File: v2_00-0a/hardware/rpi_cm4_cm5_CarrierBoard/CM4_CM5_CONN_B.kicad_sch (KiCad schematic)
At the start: 2 parts, among them J7 DF40HC(3.0)-100DS-0.4V(58), U17 Raspberry PI CM4 and CM5 symb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

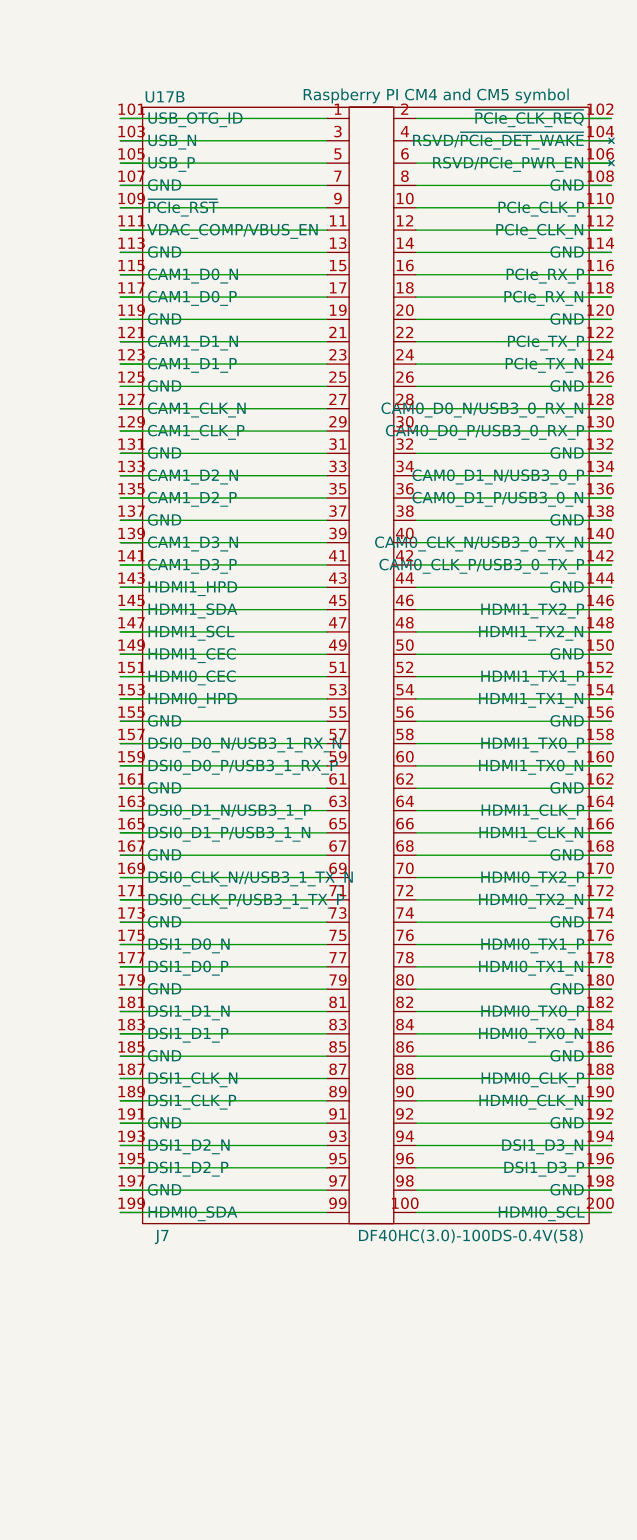
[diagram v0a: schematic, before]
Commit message: Update schematics (several new hierarchical pages, updates bus labels)
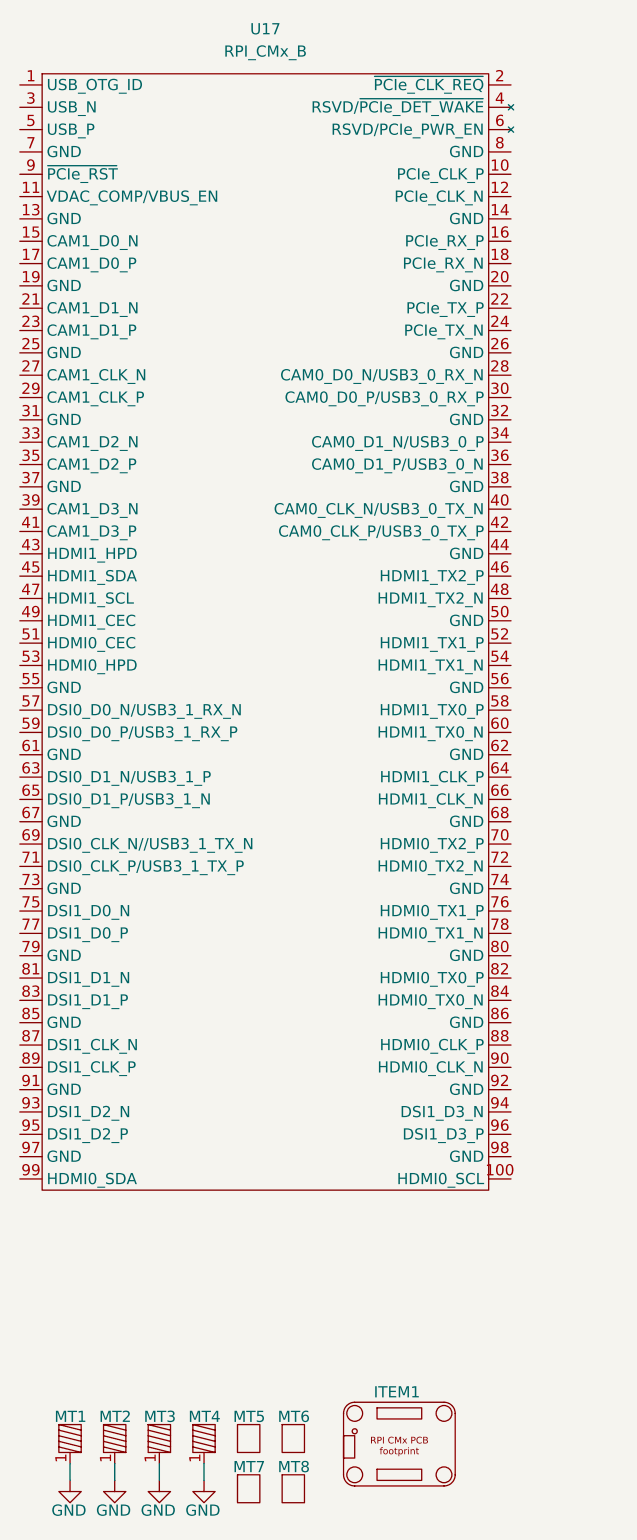
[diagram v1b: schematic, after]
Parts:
- removed J7: DF40HC(3.0)-100DS-0.4V(58), footprint:DF40HC(3.0)-100DS-0.4V, symbol KicadCompDb:Connector/CONN_00007
- removed U17: Raspberry PI CM4 and CM5 symbol, rPI_CM4_CM5, symbol KiCad_Lib_Symbols:RPI_CM4_CM5
- added ITEM1: Raspberry PI CM4 and CM5 symbol, rPI_CM4_CM5, symbol KiCad_Lib_Symbols:RPI_CMx_PCB_FP
- added MT1, MT2, MT3, MT4: 9774030151R, footprint:9774030151R, symbol KicadCompDb:Miscellaneous/MISC_00002
- added MT5, MT6, MT7, MT8: M0504-25-AL-7, footprint:M0504-25-AL-7, symbol KicadCompDb:Miscellaneous/MISC_00004
- added U17: RPI_CMx_B, footprint:DF40HC(3.0)-100DS-0.4V, symbol KicadCompDb:Connector/CONN_00015
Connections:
- new net GND: MT1.1, MT2.1, MT3.1, MT4.1

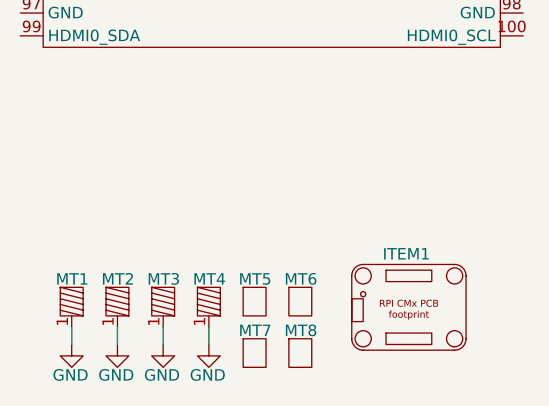
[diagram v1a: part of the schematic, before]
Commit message: Add new page and update schematics
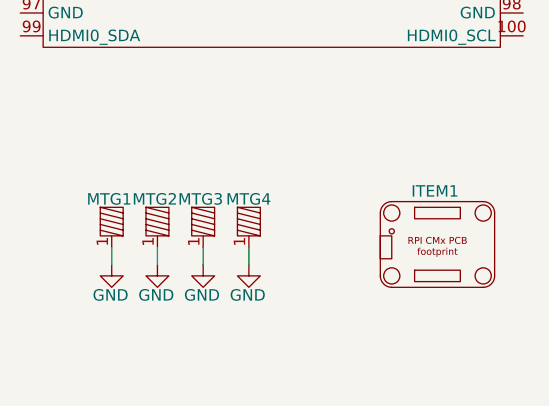
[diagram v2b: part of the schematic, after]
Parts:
- removed MT5, MT6, MT7, MT8: M0504-25-AL-7, footprint:M0504-25-AL-7, symbol KicadCompDb:Miscellaneous/MISC_00004
- renumbered MT1 to MTG1, MT2 to MTG2, MT3 to MTG3, MT4 to MTG4
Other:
- moved on the sheet: ITEM1, MTG1, MTG2, MTG3, MTG4

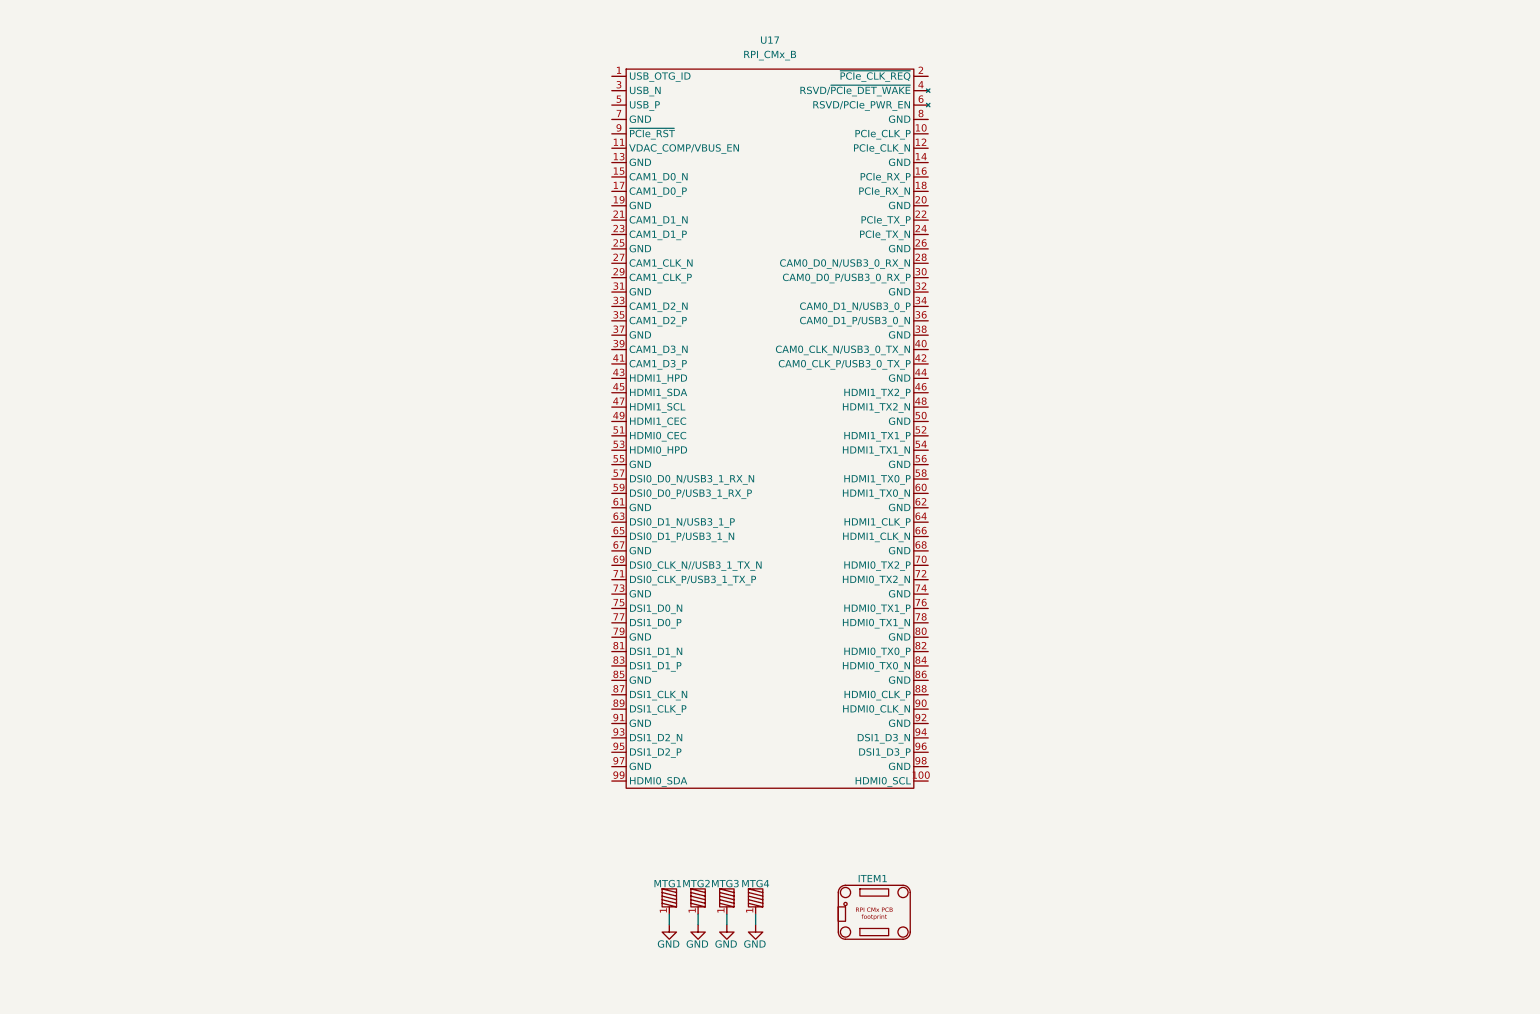
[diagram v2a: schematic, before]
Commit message: Add design notes (power table) and latest changes to power supply and power input
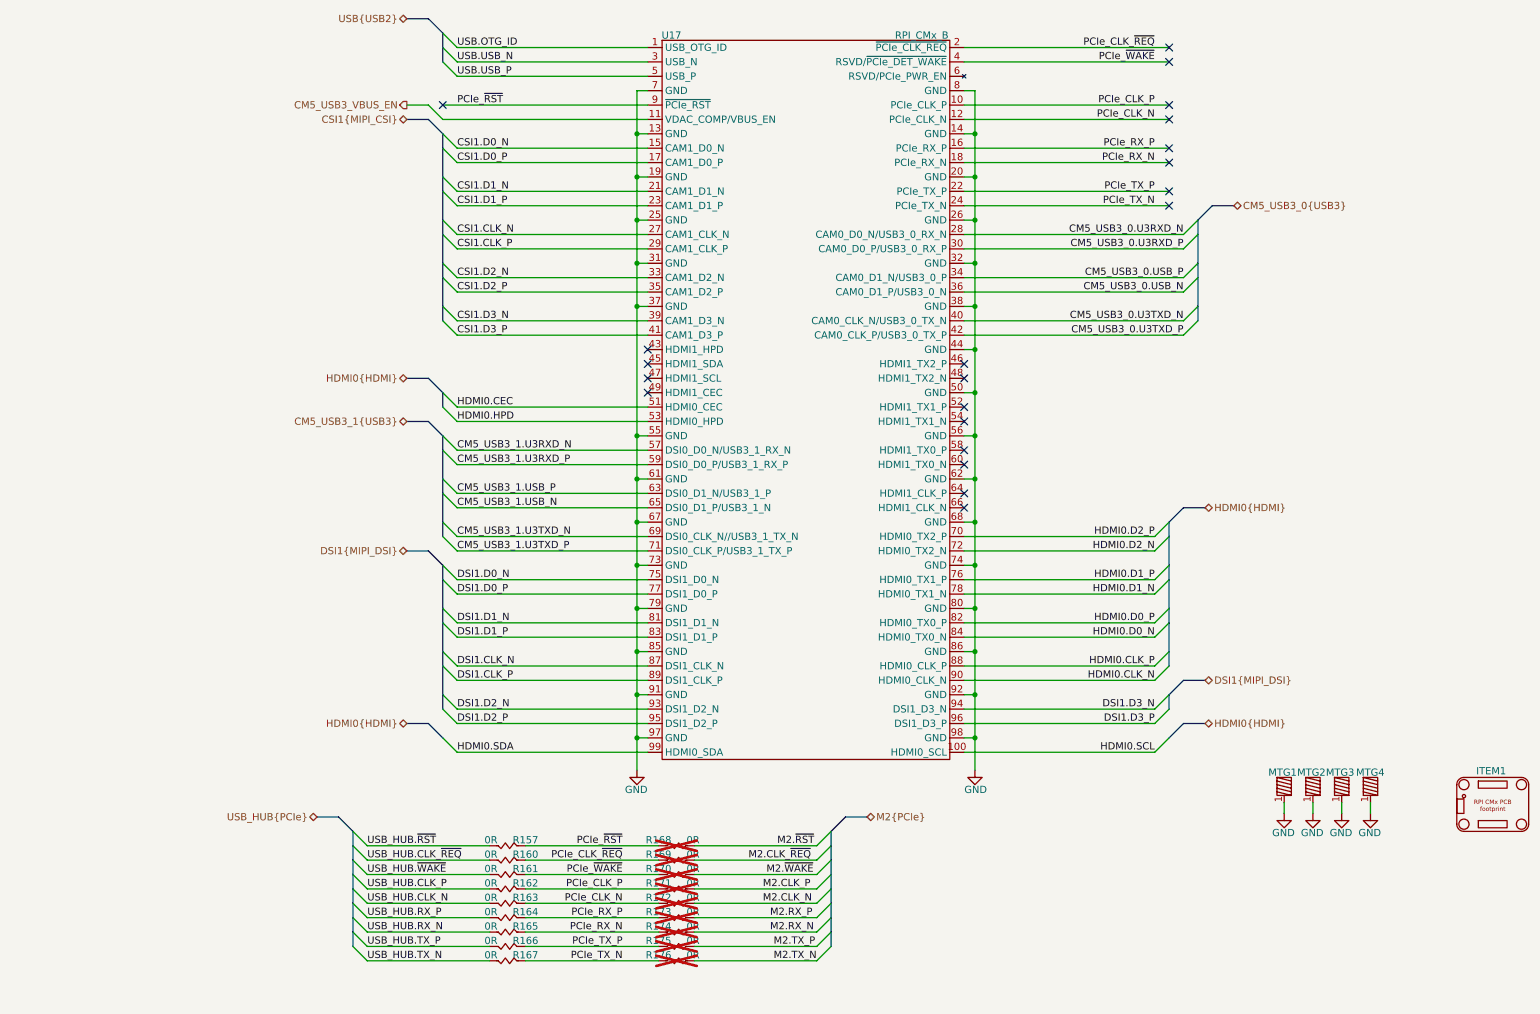
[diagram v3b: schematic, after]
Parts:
- added R157, R160, R161, R162, R163, R164, R165, R166, R167, R168, R169, R170, R171, R172, R173, R174, R175, R176: 0R, footprint:RES_0402, symbol KicadCompDb:Resistors/RES_SMT_00001
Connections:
- net GND: now also U17.13 (GND), U17.14 (GND), U17.19 (GND), U17.20 (GND), U17.25 (GND), U17.26 (GND), U17.31 (GND), U17.32 (GND), U17.37 (GND), U17.38 (GND), U17.44 (GND), U17.50 (GND), U17.55 (GND), U17.56 (GND), U17.61 (GND), U17.62 (GND), U17.67 (GND), U17.68 (GND), U17.7 (GND), U17.73 (GND), U17.74 (GND), U17.79 (GND), U17.8 (GND), U17.80 (GND), U17.85 (GND), U17.86 (GND), U17.91 (GND), U17.92 (GND), U17.97 (GND), U17.98 (GND)
- net USB.OTG_ID: now reaches U17.1 (USB_OTG_ID)
- net PCIe_CLK_P: now reaches U17.10 (PCIe_CLK_P)
- net PCIe_CLK_P: now also R162.1, R171.1
- net HDMI0.SCL: now reaches U17.100 (HDMI0_SCL)
- net CM5_USB3_VBUS_EN: now reaches U17.11 (VDAC_COMP/VBUS_EN)
- net PCIe_CLK_N: now reaches U17.12 (PCIe_CLK_N)
- net PCIe_CLK_N: now also R163.1, R172.1
- net CSI1.D0_N: now reaches U17.15 (CAM1_D0_N)
- net PCIe_RX_P: now reaches U17.16 (PCIe_RX_P)
- net PCIe_RX_P: now also R164.1, R173.1
- net CSI1.D0_P: now reaches U17.17 (CAM1_D0_P)
- net PCIe_RX_N: now reaches U17.18 (PCIe_RX_N)
- net PCIe_RX_N: now also R165.1, R174.1
- net PCIe_CLK_~{REQ}: now reaches U17.2 (~{PCIe_CLK_REQ})
- net PCIe_CLK_~{REQ}: now also R160.1, R169.1
- net CSI1.D1_N: now reaches U17.21 (CAM1_D1_N)
- net PCIe_TX_P: now reaches U17.22 (PCIe_TX_P)
- net PCIe_TX_P: now also R166.1, R175.1
- net CSI1.D1_P: now reaches U17.23 (CAM1_D1_P)
- net PCIe_TX_N: now reaches U17.24 (PCIe_TX_N)
- net PCIe_TX_N: now also R167.1, R176.1
- net CSI1.CLK_N: now reaches U17.27 (CAM1_CLK_N)
- net CM5_USB3_0.U3RXD_N: now reaches U17.28 (CAM0_D0_N/USB3_0_RX_N)
- net CSI1.CLK_P: now reaches U17.29 (CAM1_CLK_P)
- net USB.USB_N: now reaches U17.3 (USB_N)
- net CM5_USB3_0.U3RXD_P: now reaches U17.30 (CAM0_D0_P/USB3_0_RX_P)
- net CSI1.D2_N: now reaches U17.33 (CAM1_D2_N)
- net CM5_USB3_0.USB_P: now reaches U17.34 (CAM0_D1_N/USB3_0_P)
- net CSI1.D2_P: now reaches U17.35 (CAM1_D2_P)
- net CM5_USB3_0.USB_N: now reaches U17.36 (CAM0_D1_P/USB3_0_N)
- net CSI1.D3_N: now reaches U17.39 (CAM1_D3_N)
- net PCIe_~{WAKE}: now reaches U17.4 (RSVD/~{PCIe_DET_WAKE})
- net PCIe_~{WAKE}: now also R161.1, R170.1
- net CM5_USB3_0.U3TXD_N: now reaches U17.40 (CAM0_CLK_N/USB3_0_TX_N)
- net CSI1.D3_P: now reaches U17.41 (CAM1_D3_P)
- net CM5_USB3_0.U3TXD_P: now reaches U17.42 (CAM0_CLK_P/USB3_0_TX_P)
- net USB.USB_P: now reaches U17.5 (USB_P)
- net HDMI0.CEC: now reaches U17.51 (HDMI0_CEC)
- net HDMI0.HPD: now reaches U17.53 (HDMI0_HPD)
- net CM5_USB3_1.U3RXD_N: now reaches U17.57 (DSI0_D0_N/USB3_1_RX_N)
- net CM5_USB3_1.U3RXD_P: now reaches U17.59 (DSI0_D0_P/USB3_1_RX_P)
- net CM5_USB3_1.USB_P: now reaches U17.63 (DSI0_D1_N/USB3_1_P)
- net CM5_USB3_1.USB_N: now reaches U17.65 (DSI0_D1_P/USB3_1_N)
- net CM5_USB3_1.U3TXD_N: now reaches U17.69 (DSI0_CLK_N//USB3_1_TX_N)
- net HDMI0.D2_P: now reaches U17.70 (HDMI0_TX2_P)
- net CM5_USB3_1.U3TXD_P: now reaches U17.71 (DSI0_CLK_P/USB3_1_TX_P)
- net HDMI0.D2_N: now reaches U17.72 (HDMI0_TX2_N)
- net DSI1.D0_N: now reaches U17.75 (DSI1_D0_N)
- net HDMI0.D1_P: now reaches U17.76 (HDMI0_TX1_P)
- net DSI1.D0_P: now reaches U17.77 (DSI1_D0_P)
- net HDMI0.D1_N: now reaches U17.78 (HDMI0_TX1_N)
- net DSI1.D1_N: now reaches U17.81 (DSI1_D1_N)
- net HDMI0.D0_P: now reaches U17.82 (HDMI0_TX0_P)
- net DSI1.D1_P: now reaches U17.83 (DSI1_D1_P)
- net HDMI0.D0_N: now reaches U17.84 (HDMI0_TX0_N)
- net DSI1.CLK_N: now reaches U17.87 (DSI1_CLK_N)
- net HDMI0.CLK_P: now reaches U17.88 (HDMI0_CLK_P)
- net DSI1.CLK_P: now reaches U17.89 (DSI1_CLK_P)
- net PCIe_~{RST}: now reaches U17.9 (~{PCIe_RST})
- net PCIe_~{RST}: now also R157.1, R168.1
- net HDMI0.CLK_N: now reaches U17.90 (HDMI0_CLK_N)
- net DSI1.D2_N: now reaches U17.93 (DSI1_D2_N)
- net DSI1.D3_N: now reaches U17.94 (DSI1_D3_N)
- net DSI1.D2_P: now reaches U17.95 (DSI1_D2_P)
- net DSI1.D3_P: now reaches U17.96 (DSI1_D3_P)
- net HDMI0.SDA: now reaches U17.99 (HDMI0_SDA)
- new net M2.CLK_N: R172.2
- new net M2.CLK_P: R171.2
- new net M2.CLK_~{REQ}: R169.2
- new net M2.RX_N: R174.2
- new net M2.RX_P: R173.2
- new net M2.TX_N: R176.2
- new net M2.TX_P: R175.2
- new net M2.~{RST}: R168.2
- new net M2.~{WAKE}: R170.2
- new net USB_HUB.CLK_N: R163.2
- new net USB_HUB.CLK_P: R162.2
- new net USB_HUB.CLK_~{REQ}: R160.2
- new net USB_HUB.RX_N: R165.2
- new net USB_HUB.RX_P: R164.2
- new net USB_HUB.TX_N: R167.2
- new net USB_HUB.TX_P: R166.2
- new net USB_HUB.~{RST}: R157.2
- new net USB_HUB.~{WAKE}: R161.2
- no-connect marks 0 -> 21
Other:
- moved on the sheet: ITEM1, MTG1, MTG2, MTG3, MTG4

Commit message: Add and modify existing schematics
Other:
- note added: "Resistors are 1% 1/16W 0402 unless otherwise noted Capacitors are 10% 50V X7R 0402 unless otherwise noted"
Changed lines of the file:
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@@
+		)
+	)
+	(text "Resistors are 1% 1/16W 0402 unless otherwise noted\nCapacitors are 10% 50V X7R 0402 unless otherwise noted"
+		(exclude_from_sim no)
+		(at 12.7 170.942 0)
+		(effects
+			(font
+				(size 1.27 1.27)
+			)
+			(justify left)
 		)
 	)
